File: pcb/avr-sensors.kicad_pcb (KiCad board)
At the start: 2 copper layers, 49 x 49 mm, 45 parts, among them CON1 BARREL_JACK, IC1 1117, IC2 328P, J2 GPIO, J3 ICSP, J6 IO, J7 OLED, U1 LMT87, U2 MS5637, U4 ENC28J60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

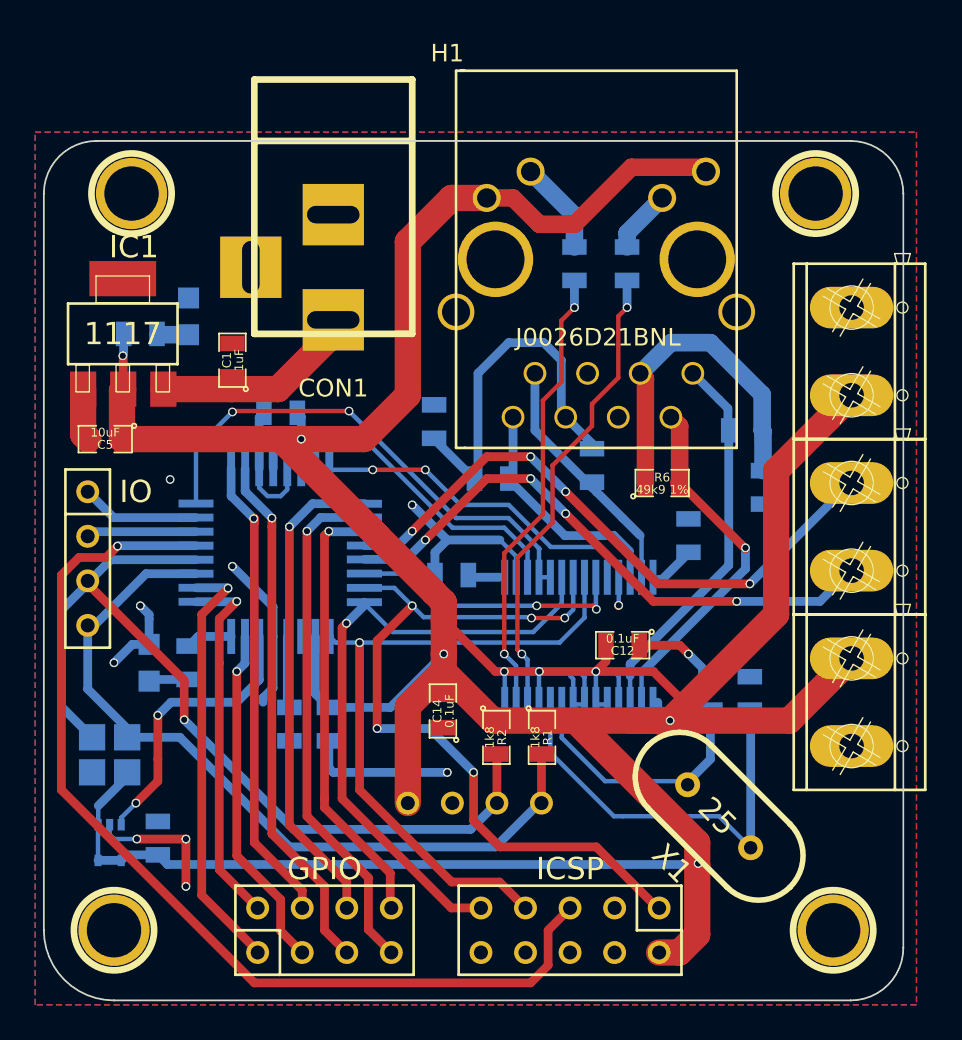
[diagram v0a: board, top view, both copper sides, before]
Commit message: pcb: Changed wrong resistor value
Value of the Ethernet termination resistors used was 49k9 instead of 49.9.
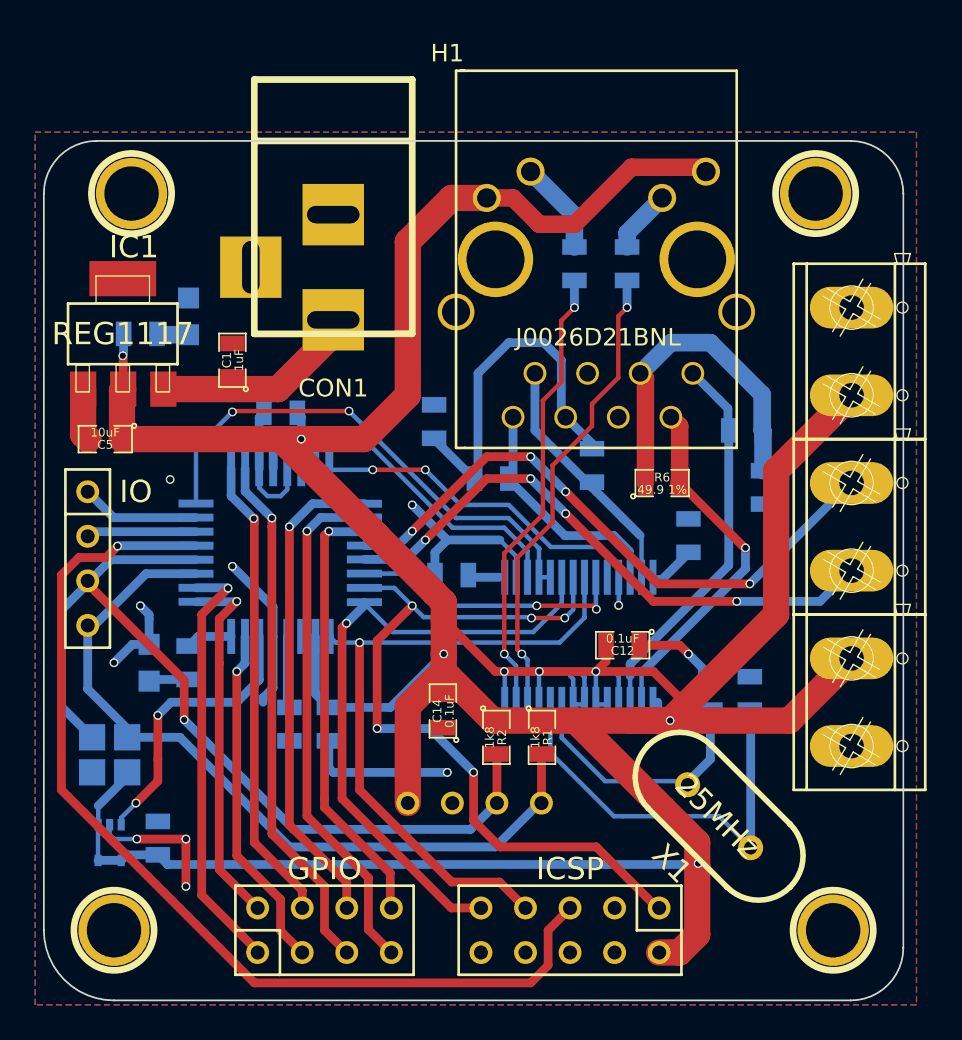
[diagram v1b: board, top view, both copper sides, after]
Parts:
- D1: value PWR -> LED-PWR
- D2: value SYS -> LED-SYS
- IC1: value 1117 -> REG1117
- IC2: value 328P -> ATMEGA328P-A
- J1: value (none) -> BUS
- J4: value (none) -> PWR-1W
- J5: value (none) -> PWR-DHT
- R5, R6, R7, R8: value 49k9 1% -> 49.9 1%
- U4: value ENC28J60 -> ENC28J60-SSOP
- X1: value 25 -> 25MHz
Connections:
- IC2 pad 19: (no net) -> Net-(IC2-Pad19)
- J3 pad 3: (no net) -> Net-(J3-Pad3)

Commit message: pcb: Changed the value of crystal capacitors to 22pF
Changed the previously undefined value of the two capacitors connected to the
25MHz crystal to 22pF.
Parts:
- C8, C9: value C -> 22pF
